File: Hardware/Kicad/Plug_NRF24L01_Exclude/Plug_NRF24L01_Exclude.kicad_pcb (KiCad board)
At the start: 2 copper layers, 40 x 30 mm, 39 parts, among them J1 Conn_02x07_Odd_Even, J2 Conn_01x08_Socket, J3 Conn_01x07_Socket, Q1 2N7002, Q2 2N7002, Q3 2N7002, Q4 2N7002, Q5 2N7002, SW1 SW_SPST, U1 STM32L412KBTx, U2 MIC5219-3.3YMM

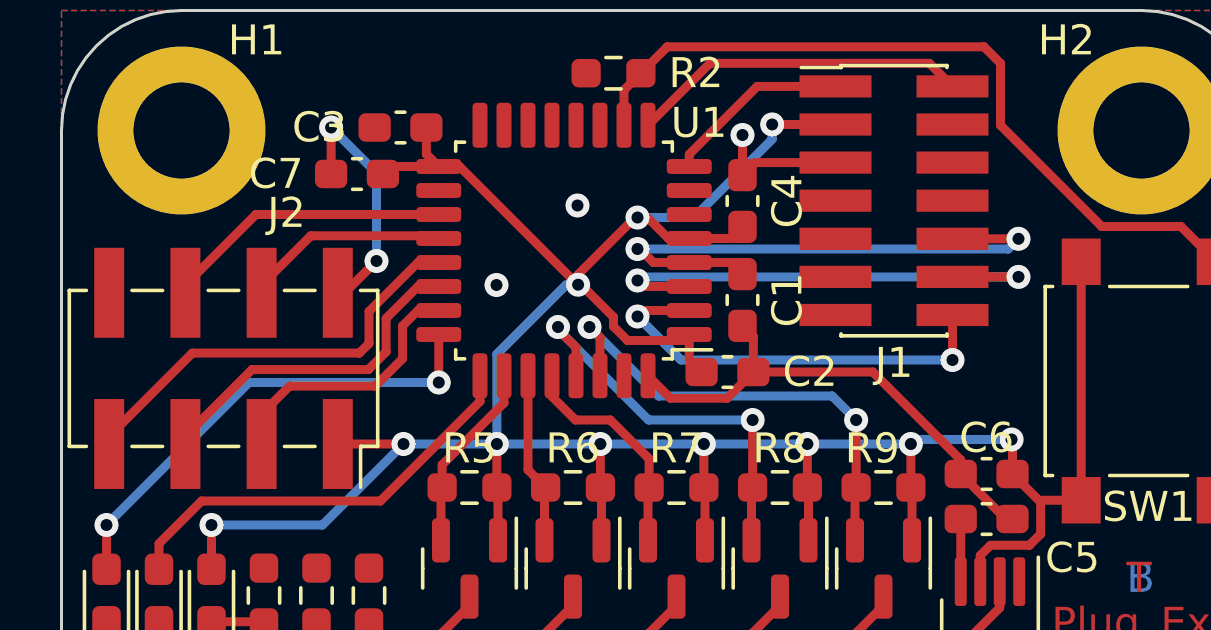
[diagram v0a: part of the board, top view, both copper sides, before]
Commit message: Update v2.2a - Plug_NRF24L01_Exclude (SWD_Connector, GND Vias) - Controller_NRF24L01_Exclude (Schematic) - Cleaned Folders
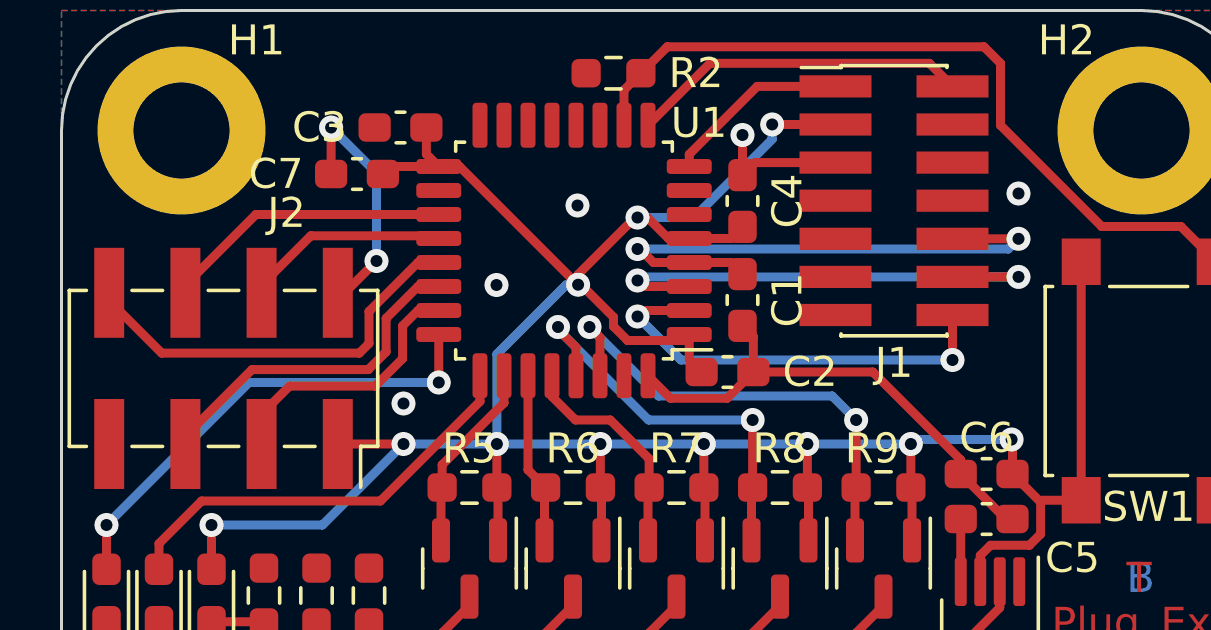
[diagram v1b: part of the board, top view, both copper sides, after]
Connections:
- J2 pad 3: Chip_Enable -> SPI_Chip_Select
- J2 pad 4: SPI_Digital_Input -> Chip_Enable
- J2 pad 5: SPI_Clock -> SPI_Digital_Output
- J2 pad 6: SPI_Digital_Output -> SPI_Clock
- J2 pad 7: SPI_Chip_Select -> unconnected-(J2-Pin_7-Pad7)
- J2 pad 8: unconnected-(J2-Pin_8-Pad8) -> SPI_Digital_Input
- U1 pad 19: SPI_Digital_Output -> SPI_Clock
- U1 pad 20: SPI_Digital_Input -> Chip_Enable
- U1 pad 21: SPI_Chip_Select -> SPI_Digital_Input
- U1 pad 22: SPI_Clock -> SPI_Digital_Output
- U1 pad 23: Chip_Enable -> SPI_Chip_Select
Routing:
- net SPI_Digital_Input: track 6.88 -> 13.8 mm
- net SPI_Chip_Select: track 14.5 -> 8.97 mm
- net Chip_Enable: track 8.97 -> 6.88 mm
- net SPI_Digital_Output: track 9.68 -> 11.7 mm
- net SPI_Clock: track 11.7 -> 9.68 mm
- net GND: vias 10 -> 12

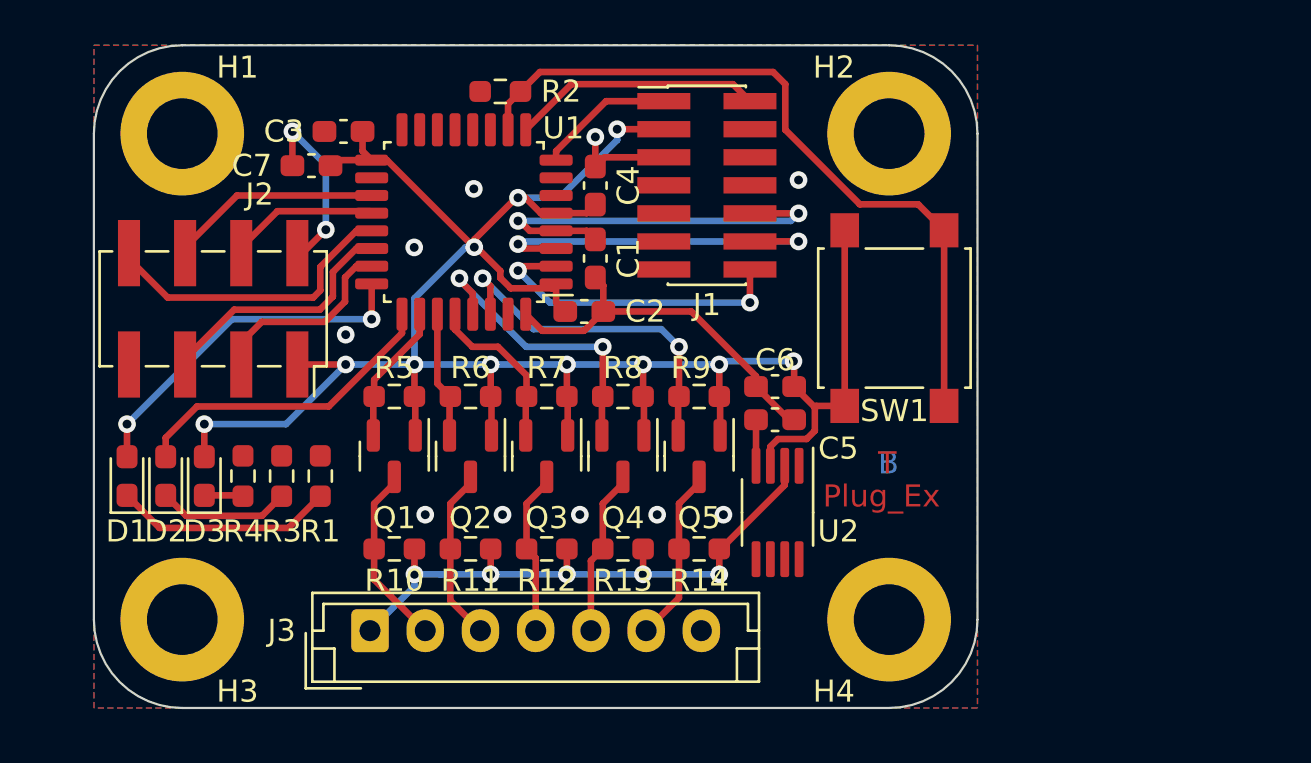
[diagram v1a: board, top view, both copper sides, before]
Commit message: Update Plug_NRF24L01 v3.0a (Warnings remaining only)
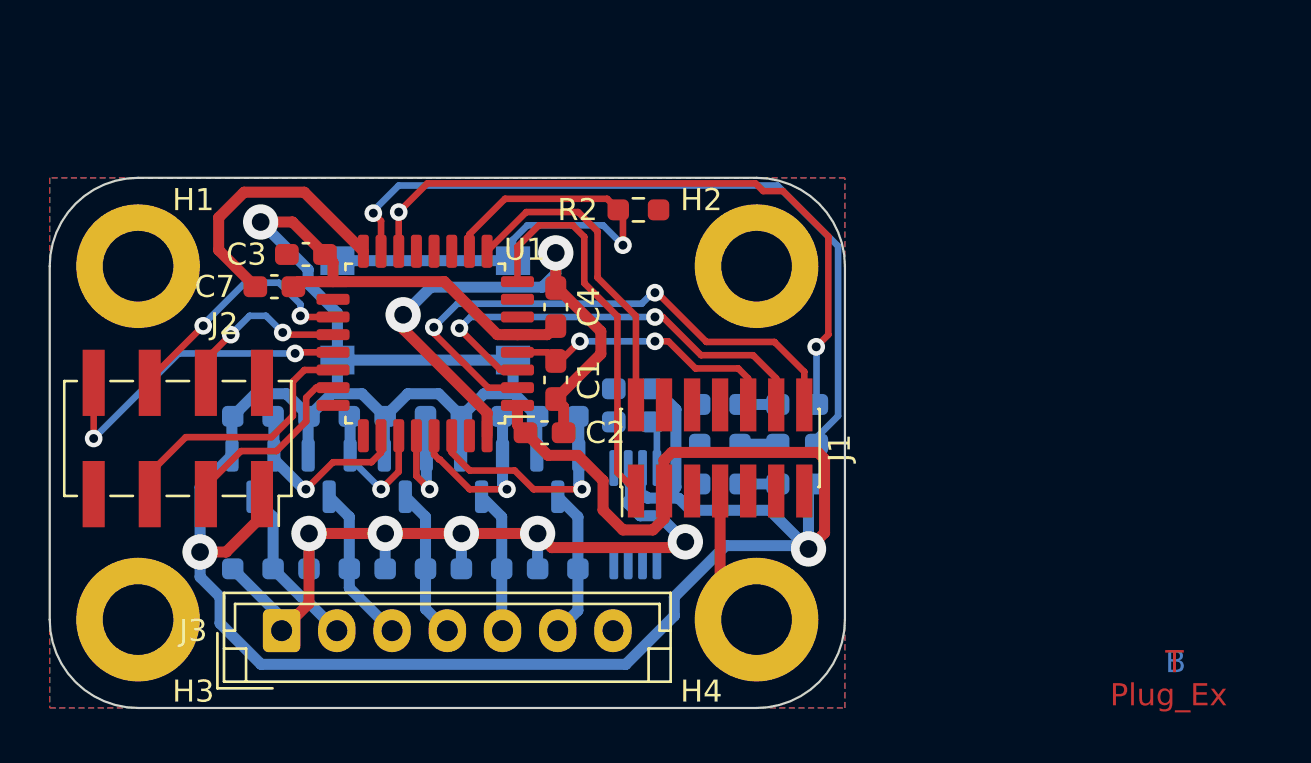
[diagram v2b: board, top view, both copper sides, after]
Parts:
- C5, C6, D1, D2, D3, Q1, Q2, Q3, Q4, Q5, R1, R10, R11, R12, R13, R14, R3, R4, R5, R6, R7, R8, R9, SW1, U2: moved to B.Cu
- moved D1 30.5 mm to (129.8, 90.3), turned to 0 degrees
- moved D2 28.6 mm to (129.8, 92.1), turned to 0 degrees
- moved D3 26.8 mm to (129.8, 93.9), turned to 0 degrees
- moved R4 21.6 mm to (126.3, 93.9), turned to 180 degrees
- moved SW1 21.2 mm to (113.0, 86.0), turned to 180 degrees
- moved R3 19.9 mm to (126.3, 92.1), turned to 180 degrees
- moved R1 18.4 mm to (126.3, 90.3), turned to 180 degrees
- moved J1 11.9 mm to (126.3, 92.2), turned to 90 degrees
- moved H2 8.49 mm to (128.0, 84.0)
- moved R2 8.23 mm to (122.7, 81.5), turned to 0 degrees
- moved Q3 6.46 mm to (112.1, 93.5)
- moved Q4 6.46 mm to (115.5, 93.5)
- moved Q5 6.46 mm to (119.0, 93.5)
- moved R12 6.46 mm to (112.1, 97.7), turned to 0 degrees
- moved R13 6.46 mm to (115.5, 97.7), turned to 0 degrees
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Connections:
- U1 pad 14: unconnected-(U1-PB0-Pad14) -> Player1_LED
- U1 pad 15: unconnected-(U1-PB1-Pad15) -> Status_LED
- U1 pad 24: Player1_LED -> unconnected-(U1-PA14-Pad24)
- U1 pad 25: Status_LED -> unconnected-(U1-PA15-Pad25)
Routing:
- net +3.3V: track 101.4 -> 149.9 mm, vias 11 -> 3
- net Status_LED: track 14.4 -> 34.0 mm, vias 0 -> 1
- net Player1_LED: track 16.1 -> 30.6 mm
- net GND: track 30.0 -> 44.1 mm, vias 12 -> 2
- net SWDCK: track 6.22 -> 17.7 mm
- net USART2_TX: track 14.4 -> 25.6 mm
- net +5V: track 28.0 -> 37.4 mm
- net Appairing_Btn: track 33.6 -> 24.6 mm, vias 0 -> 1
- net Net-(D1-K): track 9.96 -> 1.71 mm
- net NRST: track 18.9 -> 13.1 mm
- net Serial_Data2_STM32: track 13.7 -> 8.20 mm, vias 2 -> 1
- net IOBit_STM32: track 16.0 -> 10.7 mm, vias 2 -> 1
- net Net-(D2-K): track 6.00 -> 1.71 mm
- net USART2_RX: track 16.8 -> 20.4 mm
- net SWDIO: track 11.3 -> 14.7 mm
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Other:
- board size 40 x 30 mm -> 36 x 24 mm

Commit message: Upadte Plug_NRF24L01_Exclude v3.0b (Completed routing / Added images)
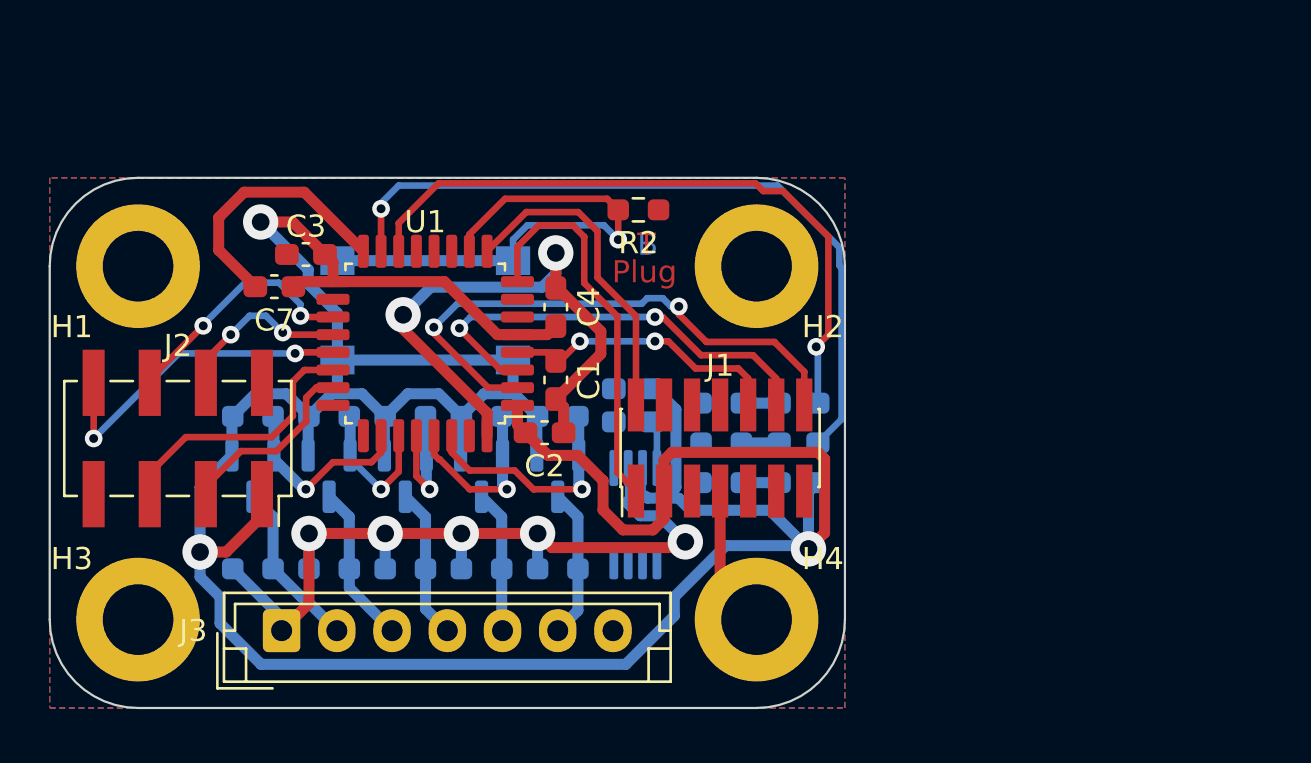
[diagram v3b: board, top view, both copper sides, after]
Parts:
- moved D1 0.08 mm to (129.9, 90.2)
- moved D2 0.08 mm to (129.9, 92.0)
- moved D3 0.08 mm to (129.9, 93.8)
- moved R1 0.08 mm to (126.4, 90.2)
- moved R3 0.08 mm to (126.4, 92.0)
- moved R4 0.08 mm to (126.4, 93.8)
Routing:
- net Appairing_Btn: track 24.6 -> 23.9 mm
- net Player1_LED: track 30.6 -> 30.3 mm, vias 2 -> 1
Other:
- board text added: "Plug"
- board text removed: "Plug_Ex"

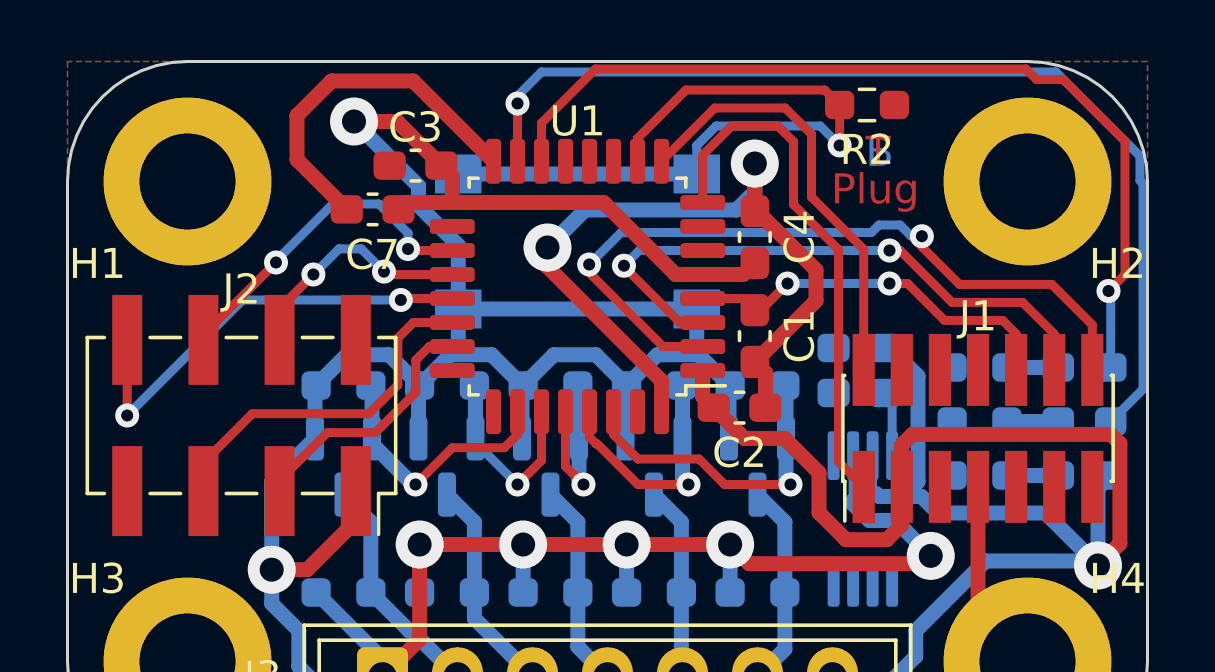
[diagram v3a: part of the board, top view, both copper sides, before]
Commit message: Update Plug_NRF24L01_Exclude v3.0b (Minor changes)
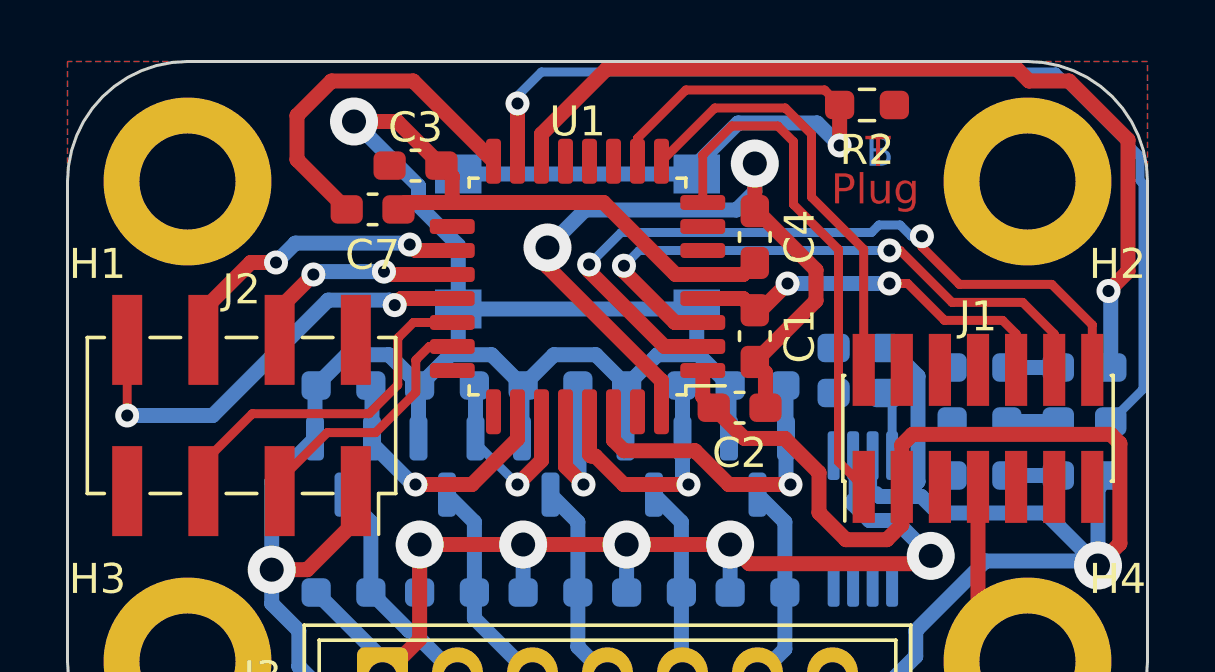
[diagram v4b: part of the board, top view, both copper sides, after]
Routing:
- net SPI_Clock: track 11.2 -> 10.3 mm
- net Chip_Enable: track 7.98 -> 7.35 mm
